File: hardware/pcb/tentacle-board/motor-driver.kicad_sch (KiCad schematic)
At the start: 21 parts, among them J5 Motor, U4 DRV8825PWP

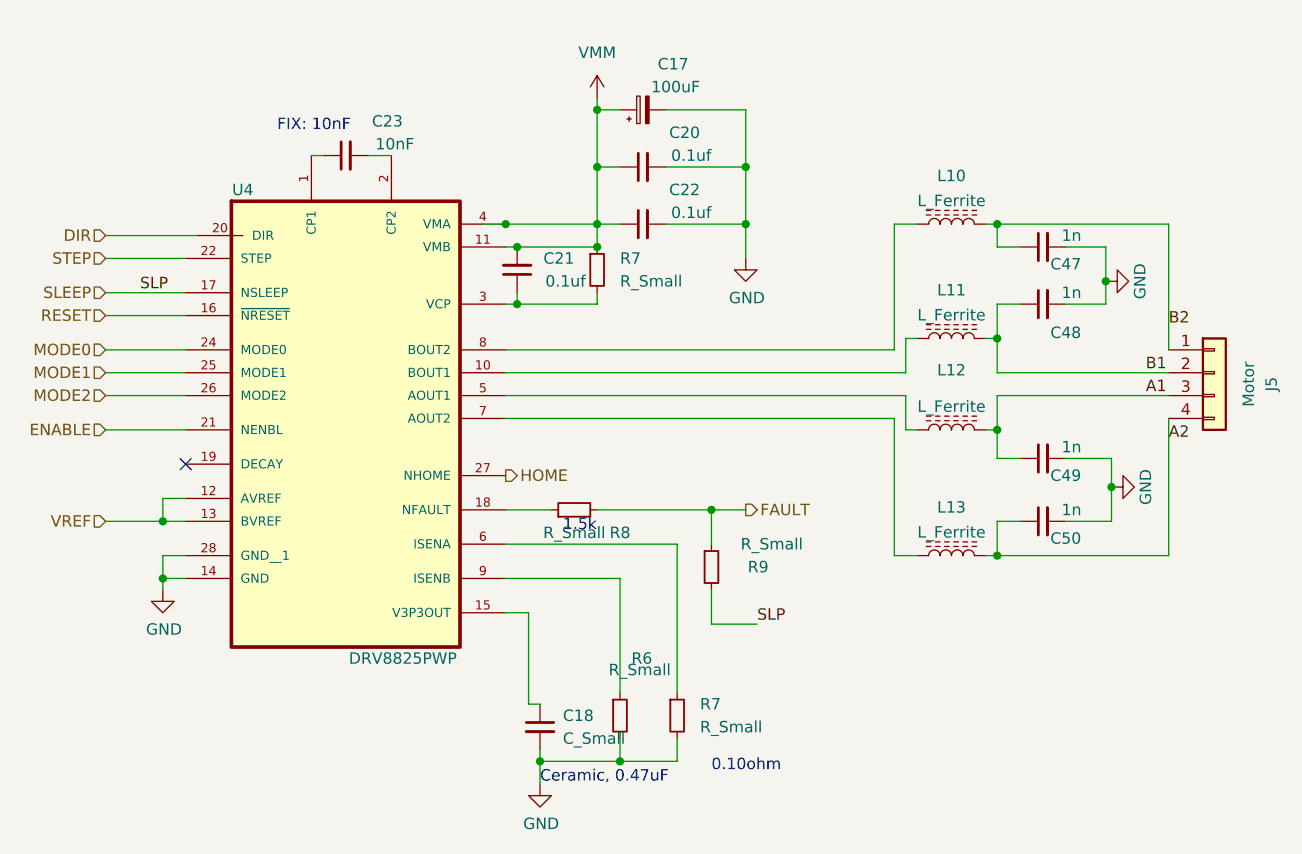
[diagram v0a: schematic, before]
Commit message: Worked on the motor power system and stepper driver BOM
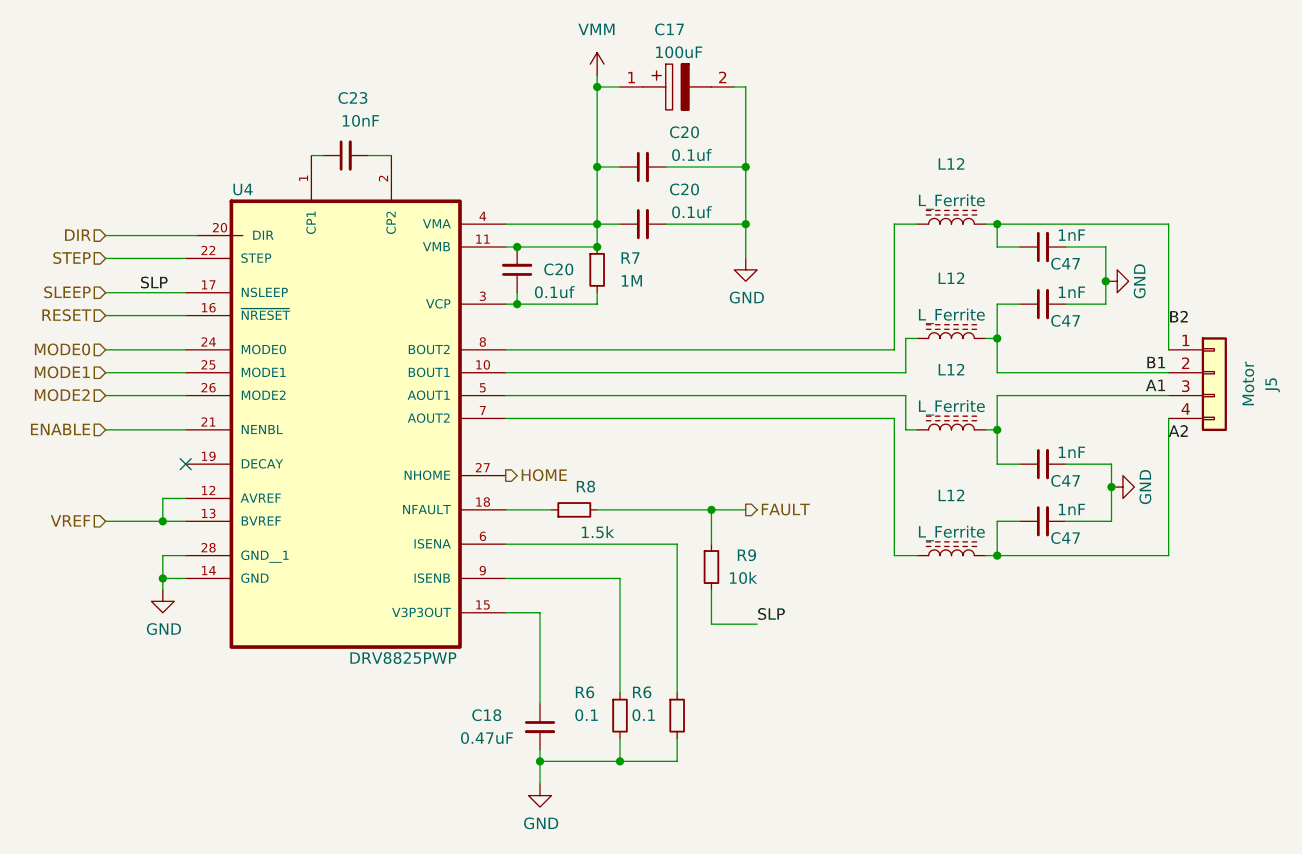
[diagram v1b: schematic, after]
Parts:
- removed C21, C22: 0.1uf, Capacitor_SMD:C_0805_2012Metric, symbol Device:C_Small
- removed C48, C49, C50: 1n, Capacitor_SMD:C_0805_2012Metric, symbol Device:C_Small
- removed L10, L11, L13: L_Ferrite, Inductor_SMD:L_0805_2012Metric, symbol Device:L_Ferrite
- removed R7: R_Small, Resistor_SMD:R_0603_1608Metric, symbol Device:R_Small
- added C20 (x2): 0.1uf, Capacitor_SMD:C_0603_1608Metric_Pad1.08x0.95mm_HandSolder, symbol Device:C_Small
- added C47 (x3): 1nF, Capacitor_SMD:C_0805_2012Metric, symbol Device:C_Small
- added L12 (x3): L_Ferrite, Inductor_SMD:L_0805_2012Metric, symbol Device:L_Ferrite
- added R6: 0.1, Resistor_SMD:R_0402_1005Metric_Pad0.72x0.64mm_HandSolder, symbol Device:R_Small
- C17: symbol Device:C_Polarized_Small -> UCD1E101MCL1GS:UCD1E101MCL1GS; LCSC # (none) -> C250945; Mfr # (none) -> UCD1E101MCL1GS; Mouser 80-EDT107M025S9HAA -> 647-UCD1E101MCL1GS
- C18: value C_Small -> 0.47uF; footprint Capacitor_SMD:C_0805_2012Metric -> Capacitor_SMD:C_0603_1608Metric; LCSC # (none) -> C577418; Mfr # (none) -> CS0603KRX7R7BB474; Mouser # (none) -> 603-CS0603KRX77BB474
- C20: footprint Capacitor_SMD:C_0805_2012Metric -> Capacitor_SMD:C_0603_1608Metric_Pad1.08x0.95mm_HandSolder; LCSC # (none) -> C3011705; Mfr # KGM21NR71H104KT -> GRM188R72A104KA35J; Mouser # 581-KGM21NR71H104KT -> 81-GRM188R72A104KA5J
- C23: footprint Capacitor_SMD:C_0805_2012Metric -> Capacitor_SMD:C_0603_1608Metric_Pad1.08x0.95mm_HandSolder; LCSC # (none) -> C100042; Mfr # KGM21NR71H104KT -> CC0603KRX7R9BB103; Mouser # 581-KGM21NR71H104KT -> 603-CC603KRX7R9BB103
- C47: value 1n -> 1nF; LCSC # (none) -> C51210; Mfr # (none) -> CL21B102KBANNNC; Mouser # (none) -> 187-CL21B102KBANNNC
- J5: LCSC # (none) -> C37815; Mfr # (none) -> XH-4A
- L12: Alt Mfr # (none) -> HCB2012KF-121T60; LCSC (none) -> C369519; Mfr # (none) -> 2508051217Y6; Mouser # (none) -> 623-2508051217Y6
- R6: value R_Small -> 0.1; footprint Resistor_SMD:R_0603_1608Metric -> Resistor_SMD:R_0402_1005Metric_Pad0.72x0.64mm_HandSolder; Alt Mfr # (none) -> FRL0402JR100TS; LCSC # (none) -> C3013344; Mfr # (none) -> RL0402FR-070R1L; Mouser # (none) -> 603-RL0402FR070R1L
- R7: value R_Small -> 1M; footprint Resistor_SMD:R_0603_1608Metric -> Resistor_SMD:R_0402_1005Metric_Pad0.72x0.64mm_HandSolder; LCSC # (none) -> C138033; Mfr # (none) -> RC0402FR-071ML; Mouser # (none) -> 603-RC0402FR-071ML
- R8: value R_Small -> 1.5k; footprint Resistor_SMD:R_0603_1608Metric -> Resistor_SMD:R_0402_1005Metric_Pad0.72x0.64mm_HandSolder; LCSC # (none) -> C114759; Mfr # (none) -> RC0402FR-071K5L; Mouser # (none) -> 603-RC0402FR-071K5L
- R9: value R_Small -> 10k; footprint Resistor_SMD:R_0603_1608Metric -> Resistor_SMD:R_0402_1005Metric_Pad0.72x0.64mm_HandSolder; LCSC # (none) -> C60490; Mfr # (none) -> RC0402FR-0710KL; Mouser # (none) -> 603-RC0402FR-0710KL
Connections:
- net A1: now also C47.1
- net A2: now also C47.1, L12.2
- net B1: now also C47.1, L12.2
- net B2: now also L12.2
- net GND: now also C20.2, C47.2, C47.2, C47.2, R6.2
- net VMM: now also C20.1, C20.2
- net at U4.10 (BOUT1): now also L12.1
- net at U4.7 (AOUT2): now also L12.1
- net at U4.6 (ISENA): now also R6.1
- net at R7.2, U4.3 (VCP): now also C20.1
- net at U4.8 (BOUT2): now also L12.1
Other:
- note removed: "0.10ohm"
- note removed: "1.5k"
- note removed: "Ceramic, 0.47uF"
- note removed: "FIX: 10nF"

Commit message: Added the MCU and supporting components and wired them up
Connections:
- net VMM renamed VDC
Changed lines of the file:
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@@
+    )
+  )
+  (symbol (lib_id "power:VDC") (at 104.14 40.64 0) (unit 1)
+    (in_bom yes) (on_board yes) (dnp no) (fields_autoplaced)
+    (property "Reference" "#PWR019" (at 104.14 43.18 0)
+      (effects (font (size 1.27 1.27)) hide)
+    )
+    (property "Value" "VDC" (at 104.14 35.56 0)
+      (effects (font (size 1.27 1.27)))
+    )
+    (property "Footprint" "" (at 104.14 40.64 0)
+      (effects (font (size 1.27 1.27)) hide)
+    )
+    (property "Datasheet" "" (at 104.14 40.64 0)
+      (effects (font (size 1.27 1.27)) hide)
+    )
+    (pin "1")
+    (instances
+      (project "tentacle-board"
+        (path "/d454cd10-f556-44dd-adb6-83df793ddd31/a708fbb2-70ed-4316-8106-f355b0ec665b"
+          (reference "#PWR019") (unit 1)
+        )
+        (path "/d454cd10-f556-44dd-adb6-83df793ddd31/77daf5cb-ccfd-4d97-90e7-081454685c3b"
+          (reference "#PWR020") (unit 1)
+        )
+      )
     )
   )
@@
         )
       )
-    )
-  )
-  (symbol (lib_id "power:VMM") (at 104.14 40.64 0) (unit 1)
-    (in_bom yes) (on_board yes) (dnp no) (fields_autoplaced)
-    (property "Reference" "#PWR028" (at 104.14 44.45 0)
-      (effects (font (size 1.27 1.27)) hide)
-    )
-    (property "Value" "VMM" (at 104.14 35.56 0)
-      (effects (font (size 1.27 1.27)))
-    )
-    (property "Footprint" "" (at 104.14 40.64 0)
-      (effects (font (size 1.27 1.27)) hide)
-    )
-    (property "Datasheet" "" (at 104.14 40.64 0)
-      (effects (font (size 1.27 1.27)) hide)
-    )
-    (pin "1")
-    (instances
-      (project "tentacle-board"
-        (path "/d454cd10-f556-44dd-adb6-83df793ddd31"
-          (reference "#PWR028") (unit 1)
-        )
-        (path "/d454cd10-f556-44dd-adb6-83df793ddd31/a708fbb2-70ed-4316-8106-f355b0ec665b"
-          (reference "#PWR027") (unit 1)
-        )
-        (path "/d454cd10-f556-44dd-adb6-83df793ddd31/77daf5cb-ccfd-4d97-90e7-081454685c3b"
-          (reference "#PWR034") (unit 1)
-        )
-      )

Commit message: Finished component & trace layout
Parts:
- U4: footprint IC_TPS61196PWPRQ1 -> tentacle-board:IC_TPS61196PWPRQ1

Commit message: Finished v1 and created manufacturing outputs
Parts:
- U4: LCSC # (none) -> C81582; Mfr # (none) -> DRV8825PWPR; Mouser # (none) -> 595-DRV8825PWPR
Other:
- company: (none) -> Squeaky Robot
- title: (none) -> Tentacle Controller Board
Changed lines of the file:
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@@
 (kicad_sch (version 20230121) (generator eeschema)
   (paper "A4")
+  (title_block
+    (title "Tentacle Controller Board")
+    (date "2023-10-24")
+    (rev "REV1")
+    (company "Squeaky Robot")
+  )
   (junction (at 120.65 57.15) (diameter 0) (color 0 0 0 0)
   )
@@
       (effects (font (size 1.27 1.27)) (justify left bottom) hide)
     )
-    (pin "1")
+    (property "Mfr #" "DRV8825PWPR" (at 76.2 90.17 0)
+      (effects (font (size 1.27 1.27)) hide)
+    )
+    (property "LCSC #" "C81582" (at 76.2 90.17 0)
+      (effects (font (size 1.27 1.27)) hide)
+    )
+    (property "Mouser #" "595-DRV8825PWPR" (at 76.2 90.17 0)
+      (effects (font (size 1.27 1.27)) hide)
+    )
+    (pin "1")
